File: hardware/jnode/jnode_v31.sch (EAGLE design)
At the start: 63 parts, among them IC1 JENNIC_JN5139, IC2 ATMEGA32U4-AUQFN44, IC3 LTC3553, IC4 LSM303DLM, IC5 L3G4200D, IC6 MPL115A, SW1 SONDER_H_VIBRATIONSSCHALTER, T1 DMP2104LP-7, X1 USB-MICROB, X2 53261-03

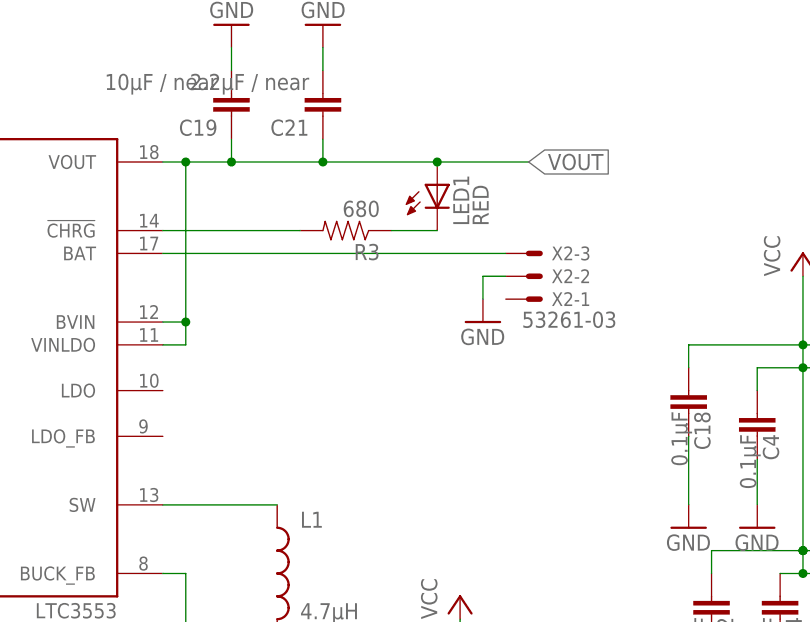
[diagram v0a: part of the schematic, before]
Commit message: add jnode_v3 layout and v31
 v31 replacess the battery connector to one compatible with the Ipod Video 5g
battery, which is almost the same size as the jNode.
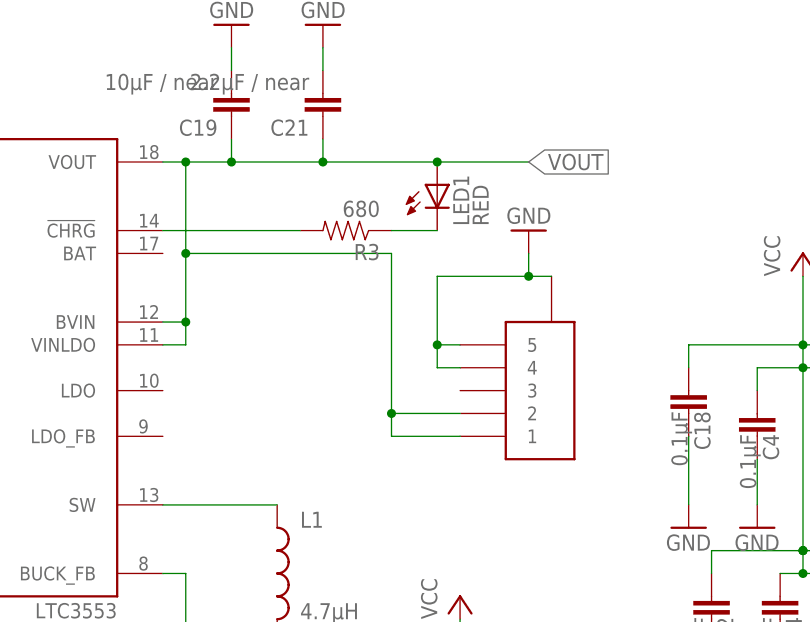
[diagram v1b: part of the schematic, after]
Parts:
- removed X2: 53261-03, con-molex:53261-03
- added U$1: SFV5R, jnode:SFV5R
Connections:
- removed net VBATT: IC3.BAT, X2-3.S
- net GND: now also U$1.4, U$1.5, U$1.P$6; no longer X2-2.S
- net VOUT: now also U$1.1, U$1.2
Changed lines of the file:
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@@
 <attribute name="DIGIKEY" value="http://search.digikey.com/scripts/DkSearch/dksus.dll?Detail&amp;name=LTC3553EUD%23PBF-ND"/>
 </part>
-<part name="GND5" library="supply1" deviceset="GND" device=""/>
 <part name="GND10" library="supply1" deviceset="GND" device=""/>
 <part name="R2" library="sparkfun" deviceset="RESISTOR" device="0402-RES" value="1.8k">
@@
 <part name="JP1" library="sparkfun" deviceset="JUMPER-2" device="SMD-NO"/>
 <part name="GND25" library="supply1" deviceset="GND" device=""/>
-<part name="X2" library="con-molex" deviceset="53?-03" device="261">
-<attribute name="IPODCONN" value="http://www.batteryspace.com/li-ionbatterymodule37v500mahwithpcb043144foripodmini185wh.aspx"/>
-</part>
 <part name="FRAME1" library="frames" deviceset="A3L-LOC" device=""/>
 <part name="P+21" library="supply1" deviceset="VCC" device=""/>
@@
 <attribute name="TECO" value="yes"/>
 </part>
+<part name="U$1" library="jnode" deviceset="SFV5R" device="">
+<attribute name="DIGIKEY" value="http://www.digikey.de/product-detail/de/SFV5R-1STE1HLF/609-4330-1-ND/2626781"/>
+<attribute name="KONTAKTE" value="unten"/>
+</part>
+<part name="GND37" library="supply1" deviceset="GND" device=""/>
 </parts>
 <sheets>
@@
 <attribute name="DIGIKEY" x="58.42" y="104.14" size="1.778" layer="96" display="off"/>
 </instance>
-<instance part="GND5" gate="1" x="116.84" y="106.68"/>
 <instance part="GND10" gate="1" x="60.96" y="55.88"/>
 <instance part="R2" gate="G$1" x="38.1" y="114.3" rot="R180">
@@
 <instance part="JP1" gate="A" x="172.72" y="111.76"/>
 <instance part="GND25" gate="1" x="167.64" y="106.68"/>
-<instance part="X2" gate="-1" x="121.92" y="109.22" rot="MR180">
-<attribute name="IPODCONN" x="121.92" y="109.22" size="1.778" layer="96" rot="MR180" display="off"/>
-</instance>
-<instance part="X2" gate="-2" x="121.92" y="111.76" rot="MR180"/>
-<instance part="X2" gate="-3" x="121.92" y="114.3" rot="MR180"/>
 <instance part="FRAME1" gate="G$1" x="0" y="0"/>
 <instance part="P+21" gate="VCC" x="292.1" y="200.66"/>
@@
 <attribute name="FARNELL" x="22.86" y="40.64" size="1.778" layer="96" rot="R270" display="off"/>
 </instance>
+<instance part="U$1" gate="G$1" x="119.38" y="91.44">
+<attribute name="DIGIKEY" x="119.38" y="91.44" size="1.778" layer="96" display="off"/>
+<attribute name="KONTAKTE" x="119.38" y="91.44" size="1.778" layer="96" display="off"/>
+</instance>
+<instance part="GND37" gate="1" x="121.92" y="116.84" rot="R180"/>
 </instances>
 <busses>
@@
 </segment>
 <segment>
-<pinref part="X2" gate="-2" pin="S"/>
-<pinref part="GND5" gate="1" pin="GND"/>
-<wire x1="119.38" y1="111.76" x2="116.84" y2="111.76" width="0.1524" layer="91"/>
-<wire x1="116.84" y1="111.76" x2="116.84" y2="109.22" width="0.1524" layer="91"/>
-</segment>
-<segment>
 <pinref part="C22" gate="G$1" pin="2"/>
 <wire x1="330.2" y1="170.18" x2="330.2" y2="167.64" width="0.1524" layer="91"/>
@@
 <wire x1="114.3" y1="195.58" x2="109.22" y2="195.58" width="0.1524" layer="91"/>
 </segment>
+<segment>
+<pinref part="U$1" gate="G$1" pin="4"/>
+<wire x1="114.3" y1="101.6" x2="111.76" y2="101.6" width="0.1524" layer="91"/>
+<wire x1="111.76" y1="101.6" x2="111.76" y2="104.14" width="0.1524" layer="91"/>
+<pinref part="U$1" gate="G$1" pin="5"/>
+<wire x1="114.3" y1="104.14" x2="111.76" y2="104.14" width="0.1524" layer="91"/>
+<pinref part="U$1" gate="G$1" pin="P$6"/>
+<wire x1="124.46" y1="111.76" x2="121.92" y2="111.76" width="0.1524" layer="91"/>
+<wire x1="121.92" y1="111.76" x2="111.76" y2="111.76" width="0.1524" layer="91"/>
+<wire x1="111.76" y1="104.14" x2="111.76" y2="111.76" width="0.1524" layer="91"/>
+<junction x="111.76" y="104.14"/>
+<pinref part="GND37" gate="1" pin="GND"/>
+<wire x1="121.92" y1="111.76" x2="121.92" y2="114.3" width="0.1524" layer="91"/>
+<junction x="121.92" y="111.76"/>
+</segment>
 </net>
 <net name="N$10" class="0">
@@
 <pinref part="R6" gate="G$1" pin="2"/>
 <pinref part="IC1" gate="G$1" pin="SPISWP"/>
-</segment>
-</net>
-<net name="VBATT" class="0">
-<segment>
-<wire x1="119.38" y1="114.3" x2="81.28" y2="114.3" width="0.1524" layer="91"/>
-<pinref part="IC3" gate="G$1" pin="BAT"/>
-<pinref part="X2" gate="-3" pin="S"/>
 </segment>
 </net>
@@
 <wire x1="88.9" y1="124.46" x2="88.9" y2="127" width="0.1524" layer="91"/>
 <junction x="88.9" y="124.46"/>
-<wire x1="83.82" y1="106.68" x2="83.82" y2="124.46" width="0.1524" layer="91"/>
+<wire x1="83.82" y1="106.68" x2="83.82" y2="114.3" width="0.1524" layer="91"/>
 <junction x="83.82" y="124.46"/>
+<wire x1="83.82" y1="114.3" x2="83.82" y2="124.46" width="0.1524" layer="91"/>
 <wire x1="99.06" y1="124.46" x2="111.76" y2="124.46" width="0.1524" layer="91"/>
 <junction x="99.06" y="124.46"/>
@@
 <wire x1="88.9" y1="124.46" x2="99.06" y2="124.46" width="0.1524" layer="91"/>
 <junction x="111.76" y="124.46"/>
-</segment>
-<segment>
+<wire x1="83.82" y1="114.3" x2="106.68" y2="114.3" width="0.1524" layer="91"/>
+<wire x1="106.68" y1="114.3" x2="106.68" y2="96.52" width="0.1524" layer="91"/>
+<junction x="83.82" y="114.3"/>
+<pinref part="U$1" gate="G$1" pin="2"/>
+<wire x1="106.68" y1="96.52" x2="114.3" y2="96.52" width="0.1524" layer="91"/>
+<pinref part="U$1" gate="G$1" pin="1"/>
+<wire x1="114.3" y1="93.98" x2="106.68" y2="93.98" width="0.1524" layer="91"/>
+<wire x1="106.68" y1="93.98" x2="106.68" y2="96.52" width="0.1524" layer="91"/>
+<junction x="106.68" y="96.52"/>
+</segment>
+<segment>
